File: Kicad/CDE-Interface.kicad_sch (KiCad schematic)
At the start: 13 parts, among them J701 CDE, U701 DRV8876

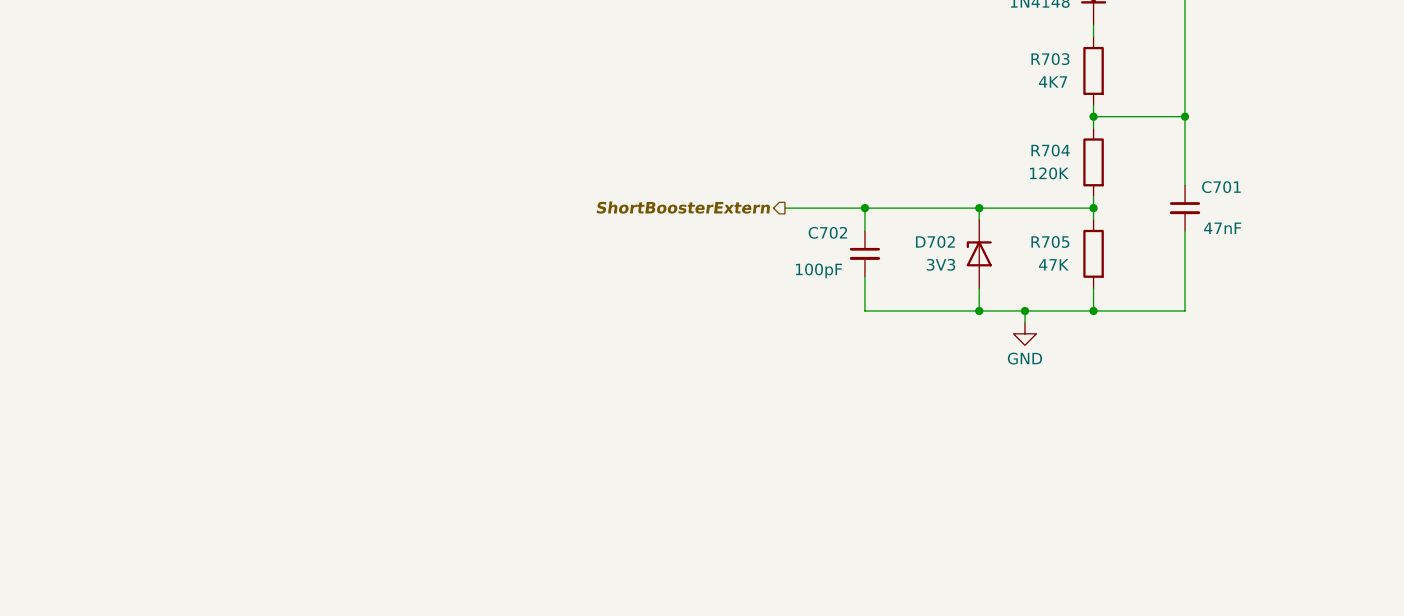
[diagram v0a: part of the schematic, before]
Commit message: Version 2.2
Version 2.2 is a small update of the CDE interface (the 3V3 zener removed, some values changed). If you already have a V2.1 board, there is no need to change: kust remove the 3V3 zener and change 2 resistor and 1 capacitor value in the CDE section
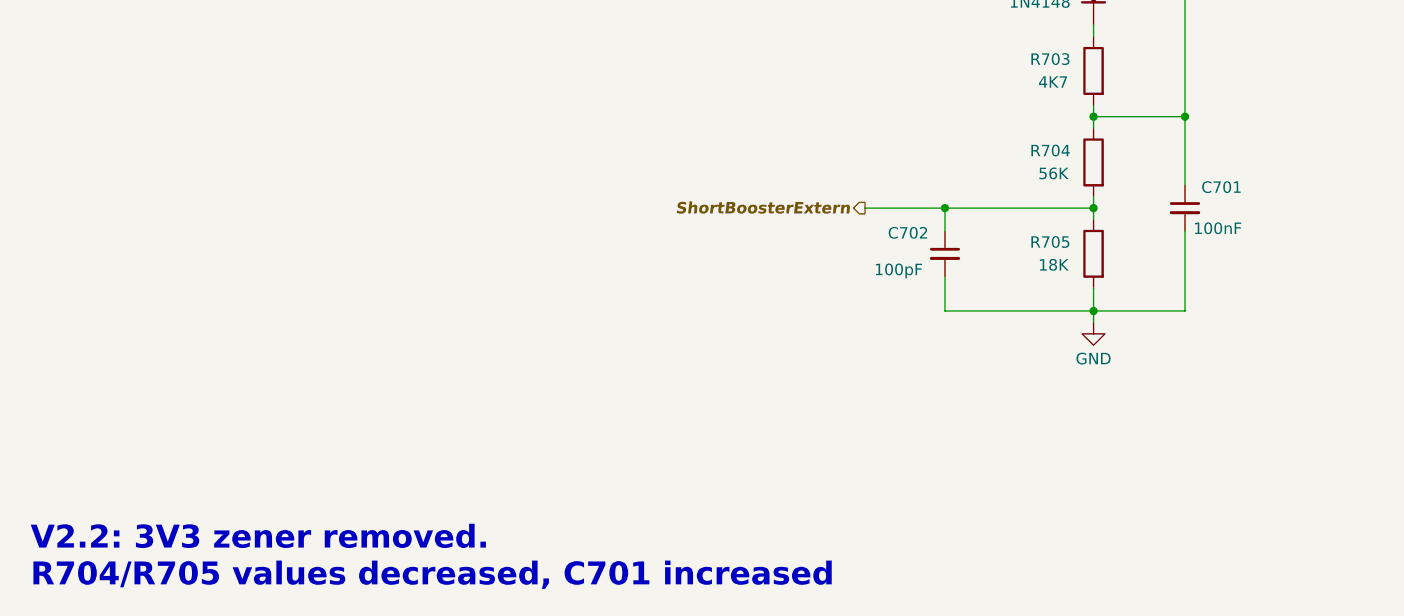
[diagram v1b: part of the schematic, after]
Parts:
- removed D702: 3V3, AP_Library:DO35-7, symbol Device:D_Zener
- C701: value 47nF -> 100nF
- R704: value 120K -> 56K
- R705: value 47K -> 18K
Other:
- note added: "V2.2: 3V3 zener removed. R704/R705 values decreased, C701 increased"
- moved on the sheet: C702

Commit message: Centrale V2.3 (1)
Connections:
- net C renamed DCC-C
- net D renamed DCC-D
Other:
- note added: "C"
- note added: "D"
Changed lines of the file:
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@@
+		)
+	)
+	(text "D"
+		(exclude_from_sim no)
+		(at 149.3806 69.85 0)
+		(effects
+			(font
+				(size 1.27 1.27)
+				(thickness 0.254)
+				(bold yes)
+				(italic yes)
+				(color 0 0 0 1)
+			)
 		)
 	)
@@
 		)
 	)
+	(text "C"
+		(exclude_from_sim no)
+		(at 149.352 66.04 0)
+		(effects
+			(font
+				(size 1.27 1.27)
+				(thickness 0.254)
+				(bold yes)
+				(italic yes)
+				(color 0 0 0 1)
+			)
+		)
+	)
 	(junction
 		(at 101.6 88.9)
@@
 	)
 	(junction
+		(at 113.03 67.31)
+		(diameter 0)
+		(color 0 0 0 0)
+	)
+	(junction
 		(at 104.14 83.82)
 		(diameter 0)
@@
 	)
 	(junction
+		(at 113.03 71.12)
+		(diameter 0)
+		(color 0 0 0 0)
+	)
+	(junction
 		(at 31.75 82.55)
 		(diameter 0)
@@
 	(wire
 		(pts
+			(xy 114.3 72.39) (xy 113.03 72.39)
+		)
+		(stroke
+			(width 0)
+			(type default)
+		)
+	)
+	(wire
+		(pts
 			(xy 116.84 151.13) (xy 133.35 151.13)
 		)
@@
 	(wire
 		(pts
+			(xy 113.03 71.12) (xy 113.03 72.39)
+		)
+		(stroke
+			(width 0)
+			(type default)
+		)
+	)
+	(wire
+		(pts
 			(xy 59.69 92.71) (xy 59.69 93.98)
 		)
@@
 	(wire
 		(pts
+			(xy 113.03 67.31) (xy 133.35 67.31)
+		)
+		(stroke
+			(width 0)
+			(type default)
+		)
+	)
+	(wire
+		(pts
 			(xy 133.35 119.38) (xy 133.35 120.65)
 		)
@@
 	(wire
 		(pts
+			(xy 113.03 66.04) (xy 113.03 67.31)
+		)
+		(stroke
+			(width 0)
+			(type default)
+		)
+	)
+	(wire
+		(pts
 			(xy 143.51 129.54) (xy 133.35 129.54)
 		)
@@
 	(wire
 		(pts
+			(xy 114.3 66.04) (xy 113.03 66.04)
+		)
+		(stroke
+			(width 0)
+			(type default)
+		)
+	)
+	(wire
+		(pts
 			(xy 58.42 71.12) (xy 62.23 71.12)
 		)
@@
 	(wire
 		(pts
-			(xy 100.33 71.12) (xy 154.94 71.12)
+			(xy 100.33 71.12) (xy 113.03 71.12)
 		)
 		(stroke
@@
 	(wire
 		(pts
-			(xy 100.33 67.31) (xy 133.35 67.31)
+			(xy 100.33 67.31) (xy 113.03 67.31)
 		)
 		(stroke
@@
 		(pts
 			(xy 31.75 78.74) (xy 31.75 82.55)
+		)
+		(stroke
+			(width 0)
+			(type default)
+		)
+	)
+	(wire
+		(pts
+			(xy 113.03 71.12) (xy 154.94 71.12)
 		)
 		(stroke
@@
 				(bold yes)
 				(italic yes)
+				(color 0 0 0 1)
 			)
 			(justify left bottom)
 		)
 	)
-	(label "D"
-		(at 148.59 71.12 0)
+	(hierarchical_label "IN1{slash}EN"
+		(shape input)
+		(at 58.42 67.31 180)
+		(effects
+			(font
+				(size 1.27 1.27)
+			)
+			(justify right)
+		)
+	)
+	(hierarchical_label "DCC-C"
+		(shape output)
+		(at 114.3 66.04 0)
 		(effects
 			(font
@@
 				(italic yes)
 			)
-			(justify left bottom)
-		)
-	)
-	(label "C"
-		(at 148.59 67.31 0)
+			(justify left)
+		)
+	)
+	(hierarchical_label "DCC-D"
+		(shape output)
+		(at 114.3 72.39 0)
 		(effects
 			(font
@@
 				(italic yes)
 			)
-			(justify left bottom)
-		)
-	)
-	(hierarchical_label "IN1{slash}EN"
-		(shape input)
-		(at 58.42 67.31 180)
-		(effects
-			(font
-				(size 1.27 1.27)
-			)
-			(justify right)
-		)
-	)
+			(justify left)
+		)
+	)
